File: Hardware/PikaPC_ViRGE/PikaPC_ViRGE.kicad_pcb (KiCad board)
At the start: 4 copper layers, 101.6 x 101.6 mm, 136 parts, among them J1 Conn_02x07_Odd_Even, J2 DIN41612_03x32_C_Split, J3 Conn_02x08_Odd_Even, J4 DE15_Socket_HighDensity_Mount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, U1 ATF1504, U10 74LS573, U12 74FCT2245, U13 74FCT2245, U14 74FCT2245, U15 74FCT2245, U2 86C325, U3 74F521, U4 T224162B, U5 T224162B, U6 T224162B, U7 T224162B, U8 74LS573, U9 74LS573, Y1 14M31818

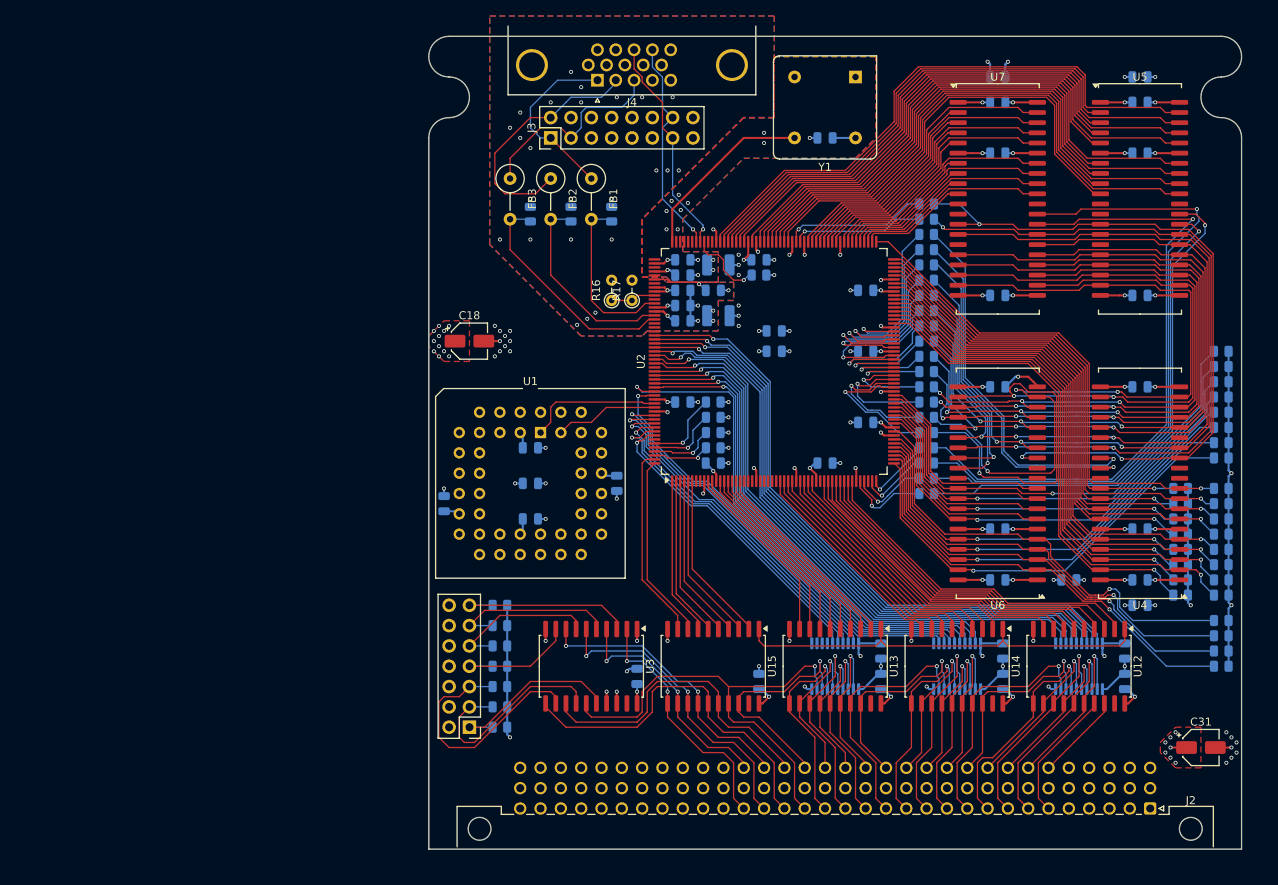
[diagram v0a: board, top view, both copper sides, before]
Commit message: ViRGE card PCB layout
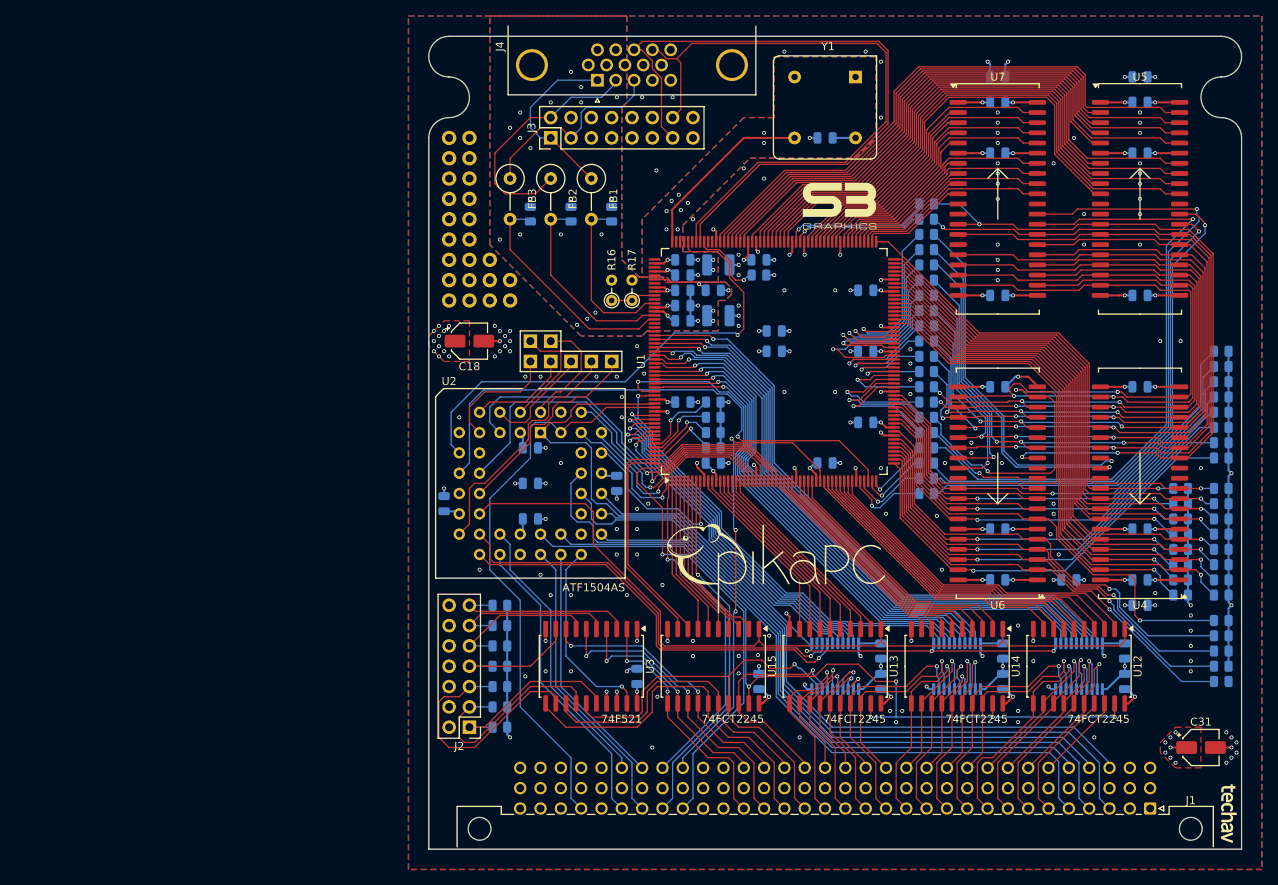
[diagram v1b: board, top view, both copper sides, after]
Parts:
- added IO11: TestPoint, Connector_PinHeader_2.54mm:PinHeader_1x01_P2.54mm_Vertical, B.Cu at (91.4, 66.0)
- added IO16: TestPoint, Connector_PinHeader_2.54mm:PinHeader_1x01_P2.54mm_Vertical, B.Cu at (94.0, 66.0)
- added IO2: TestPoint, Connector_PinHeader_2.54mm:PinHeader_1x01_P2.54mm_Vertical, B.Cu at (88.9, 63.5)
- added IO24: TestPoint, Connector_PinHeader_2.54mm:PinHeader_1x01_P2.54mm_Vertical, B.Cu at (96.5, 66.0)
- added IO30: TestPoint, Connector_PinHeader_2.54mm:PinHeader_1x01_P2.54mm_Vertical, B.Cu at (99.1, 66.0)
- added IO44: TestPoint, Connector_PinHeader_2.54mm:PinHeader_1x01_P2.54mm_Vertical, B.Cu at (91.4, 63.5)
- added IO5: TestPoint, Connector_PinHeader_2.54mm:PinHeader_1x01_P2.54mm_Vertical, B.Cu at (88.9, 66.0)
- added REF**: PinHeader_1x01_P2.54mm_Vertical, Connector_PinHeader_2.54mm:PinHeader_1x01_P2.54mm_Vertical, F.Cu at (78.7, 43.2)
- added REF**: PinHeader_1x01_P2.54mm_Vertical, Connector_PinHeader_2.54mm:PinHeader_1x01_P2.54mm_Vertical, F.Cu at (81.3, 45.7)
- added REF**: PinHeader_1x01_P2.54mm_Vertical, Connector_PinHeader_2.54mm:PinHeader_1x01_P2.54mm_Vertical, F.Cu at (78.7, 38.1)
- added REF**: PinHeader_1x01_P2.54mm_Vertical, Connector_PinHeader_2.54mm:PinHeader_1x01_P2.54mm_Vertical, F.Cu at (78.7, 48.3)
- added REF**: PinHeader_1x01_P2.54mm_Vertical, Connector_PinHeader_2.54mm:PinHeader_1x01_P2.54mm_Vertical, F.Cu at (78.7, 50.8)
- added REF**: PinHeader_1x01_P2.54mm_Vertical, Connector_PinHeader_2.54mm:PinHeader_1x01_P2.54mm_Vertical, F.Cu at (86.4, 58.4)
- added REF**: PinHeader_1x01_P2.54mm_Vertical, Connector_PinHeader_2.54mm:PinHeader_1x01_P2.54mm_Vertical, F.Cu at (81.3, 48.3)
- added REF**: PinHeader_1x01_P2.54mm_Vertical, Connector_PinHeader_2.54mm:PinHeader_1x01_P2.54mm_Vertical, F.Cu at (81.3, 43.2)
- added REF**: PinHeader_1x01_P2.54mm_Vertical, Connector_PinHeader_2.54mm:PinHeader_1x01_P2.54mm_Vertical, F.Cu at (81.3, 55.9)
- added REF**: PinHeader_1x01_P2.54mm_Vertical, Connector_PinHeader_2.54mm:PinHeader_1x01_P2.54mm_Vertical, F.Cu at (78.7, 55.9)
- added REF**: PinHeader_1x01_P2.54mm_Vertical, Connector_PinHeader_2.54mm:PinHeader_1x01_P2.54mm_Vertical, F.Cu at (81.3, 50.8)
- added REF**: PinHeader_1x01_P2.54mm_Vertical, Connector_PinHeader_2.54mm:PinHeader_1x01_P2.54mm_Vertical, F.Cu at (78.7, 58.4)
- added REF**: PinHeader_1x01_P2.54mm_Vertical, Connector_PinHeader_2.54mm:PinHeader_1x01_P2.54mm_Vertical, F.Cu at (83.8, 53.3)
- added REF**: PinHeader_1x01_P2.54mm_Vertical, Connector_PinHeader_2.54mm:PinHeader_1x01_P2.54mm_Vertical, F.Cu at (81.3, 53.3)
- added REF**: PinHeader_1x01_P2.54mm_Vertical, Connector_PinHeader_2.54mm:PinHeader_1x01_P2.54mm_Vertical, F.Cu at (78.7, 45.7)
- added REF**: PinHeader_1x01_P2.54mm_Vertical, Connector_PinHeader_2.54mm:PinHeader_1x01_P2.54mm_Vertical, F.Cu at (78.7, 40.6)
- added REF**: PinHeader_1x01_P2.54mm_Vertical, Connector_PinHeader_2.54mm:PinHeader_1x01_P2.54mm_Vertical, F.Cu at (83.8, 55.9)
- added REF**: PinHeader_1x01_P2.54mm_Vertical, Connector_PinHeader_2.54mm:PinHeader_1x01_P2.54mm_Vertical, F.Cu at (81.3, 38.1)
- added REF**: PinHeader_1x01_P2.54mm_Vertical, Connector_PinHeader_2.54mm:PinHeader_1x01_P2.54mm_Vertical, F.Cu at (78.7, 53.3)
- added REF**: PinHeader_1x01_P2.54mm_Vertical, Connector_PinHeader_2.54mm:PinHeader_1x01_P2.54mm_Vertical, F.Cu at (81.3, 40.6)
- added REF**: PinHeader_1x01_P2.54mm_Vertical, Connector_PinHeader_2.54mm:PinHeader_1x01_P2.54mm_Vertical, F.Cu at (81.3, 58.4)
- added REF**: PinHeader_1x01_P2.54mm_Vertical, Connector_PinHeader_2.54mm:PinHeader_1x01_P2.54mm_Vertical, F.Cu at (83.8, 58.4)
- added REF**: PinHeader_1x01_P2.54mm_Vertical, Connector_PinHeader_2.54mm:PinHeader_1x01_P2.54mm_Vertical, F.Cu at (86.4, 55.9)
- added SR28: 10K, Resistor_SMD:R_0805_2012Metric, B.Cu at (175.3, 98.4)
- U10, U8, U9: value 74LS573 -> 74AHCT573
- U2: renamed from U1; value ATF1504 -> ATF1504AS
- moved SR24 1.91 mm to (175.3, 106.0)
- moved SR25 1.91 mm to (175.3, 104.1)
- moved SR26 1.91 mm to (175.3, 102.2)
- moved SR27 1.91 mm to (175.3, 100.3)
- renumbered J2 to J1, J1 to J2, R38 to SR00, R39 to SR01, R40 to SR02, R41 to SR03, R42 to SR04, R43 to SR05, R44 to SR06, R45 to SR07, R46 to SR08, R47 to SR09, R48 to SR10, R49 to SR11, R50 to SR12, R51 to SR13, R52 to SR14, R53 to SR15, R54 to SR16, R55 to SR17, R56 to SR18, R57 to SR19, R58 to SR20, R59 to SR21, R60 to SR22, R61 to SR23, R62 to SR24, R63 to SR25, R64 to SR26, R65 to SR27, U2 to U1
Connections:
- U2 pad 11: /Main Bus/~{Bus-IRQ1} -> /Main Bus/VID-SAUP2
- U2 pad 12: /Main Bus/~{Bus-IRQ0} -> /Main Bus/~{OE}
- U2 pad 14: /Main Bus/~{AEN} -> Net-(U2A-IO30)
- U2 pad 17: /Main Bus/~{BEN} -> Net-(U2A-IO24)
- U2 pad 18: /Main Bus/~{Bus-Start} -> /Main Bus/A23
- U2 pad 19: /Main Bus/~{Bus-ACK} -> /Main Bus/A24
- U2 pad 2: unconnected-(U1A-OE2/GCLK2-Pad2) -> Net-(U2A-OE2/GCLK2)
- U2 pad 20: /Main Bus/Bus-R/~{W} -> /Main Bus/~{Bus-ACK}
- U2 pad 21: unconnected-(U1A-IO17-Pad21) -> /Main Bus/~{Bus-Start}
- U2 pad 24: /Main Bus/VID-SAUP1 -> /Main Bus/~{Bus-BURST}
- U2 pad 25: /Main Bus/VID-SAUP2 -> /Main Bus/~{BEN}
- U2 pad 26: /Main Bus/A23 -> /Main Bus/~{Bus-BRACK}
- U2 pad 27: /Main Bus/A24 -> /Main Bus/~{Bus-IRQ2}
- U2 pad 29: /Main Bus/VID-M/~{IO} -> /Main Bus/~{Bus-IRQ1}
- U2 pad 31: /Main Bus/~{OE} -> /Main Bus/~{Bus-IRQ0}
- U2 pad 33: /Main Bus/~{VID-ADS} -> /Main Bus/~{AEN}
- U2 pad 34: /Main Bus/~{VID-RDYIN} -> /Main Bus/~{Bus-IACK}
- U2 pad 36: /Main Bus/~{VID-SRDY} -> /Main Bus/Bus-R/~{W}
- U2 pad 37: /Main Bus/INT0 -> /Main Bus/VID-M/~{IO}
- U2 pad 39: unconnected-(U1A-IO57-Pad39) -> /Main Bus/~{VID-RDYIN}
- U2 pad 4: unconnected-(U1A-IO16-Pad4) -> Net-(U2A-IO16)
- U2 pad 40: unconnected-(U1A-IO62-Pad40) -> /Main Bus/~{VID-SRDY}
- U2 pad 41: unconnected-(U1A-IO64-Pad41) -> /Main Bus/~{VID-ADS}
- U2 pad 44: unconnected-(U1A-OE1-Pad44) -> Net-(U2A-OE1)
- U2 pad 5: /Main Bus/~{Bus-BRACK} -> /Main Bus/VID-SAUP1
- U2 pad 6: /Main Bus/~{Bus-BURST} -> Net-(U2A-IO11)
- U2 pad 8: /Main Bus/~{Bus-IACK} -> Net-(U2A-IO5)
- U2 pad 9: /Main Bus/~{Bus-IRQ2} -> /Main Bus/INT0
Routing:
- net /Main Bus/~{BEN}: track 0.00 -> 102.0 mm, vias 0 -> 5
- net /Main Bus/~{Bus-Reset}: track 17.0 -> 112.9 mm
- net /Main Bus/Bus-R/~{W}: track 0.00 -> 86.8 mm
- net /Main Bus/~{Bus-IRQ0}: track 0.00 -> 85.5 mm
- net /Main Bus/~{Bus-IRQ2}: track 0.00 -> 84.8 mm
- net /Main Bus/~{Bus-IACK}: track 0.00 -> 83.8 mm
- net /Main Bus/~{Bus-IRQ1}: track 0.00 -> 82.1 mm
- net /Main Bus/~{Bus-BE1}: track 0.00 -> 73.9 mm, vias 0 -> 1
- net /Main Bus/~{AEN}: track 0.00 -> 68.9 mm, vias 0 -> 3
- net /Main Bus/VID-SAUP2: track 0.00 -> 68.1 mm, vias 0 -> 1
- net /Main Bus/INT0: track 0.00 -> 62.3 mm, vias 0 -> 1
- net /Main Bus/Bus-Clk: track 13.0 -> 72.1 mm
- net /Video/Vid-H: track 27.7 -> 86.2 mm, vias 1 -> 0
- net /Main Bus/~{Bus-BE0}: track 0.00 -> 58.2 mm, vias 0 -> 3
- net /Main Bus/~{Bus-BE2}: track 0.00 -> 55.7 mm, vias 0 -> 1
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- added copper zone on B.Cu, net GND
- added copper zone on F.Cu, net GND
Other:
- board text added: "33Ω"
- board text added: "75Ω"
- board text added: "SR[01:00] Bus Select SR[03:02] Page Mode SR[04] Enable VBIOS SR[07:05] VRAM Size SR[08] VGA Enable SR[09] Reserved SR[10] VBIOS Size SR[11] DCLK/MCLK Src SR[12] RAMDAC ~{LOCA}"
- board text added: "SR[15:15] Reserved SR[17:16] ~{CAS}/~{OE} Adjust SR[18] ~{RAS} Timing SR[19] ~{RAS} Pre-charge SR[23:20] Reserved SR[24] Trio LPB Mode SR[25] Serial Address SR[26] MMIO Serial SR[28:27] ~{WE} Delay"
- board text added: "Strapping Options (10kΩ)"

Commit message: Un-assign main bus pins 22 & 23
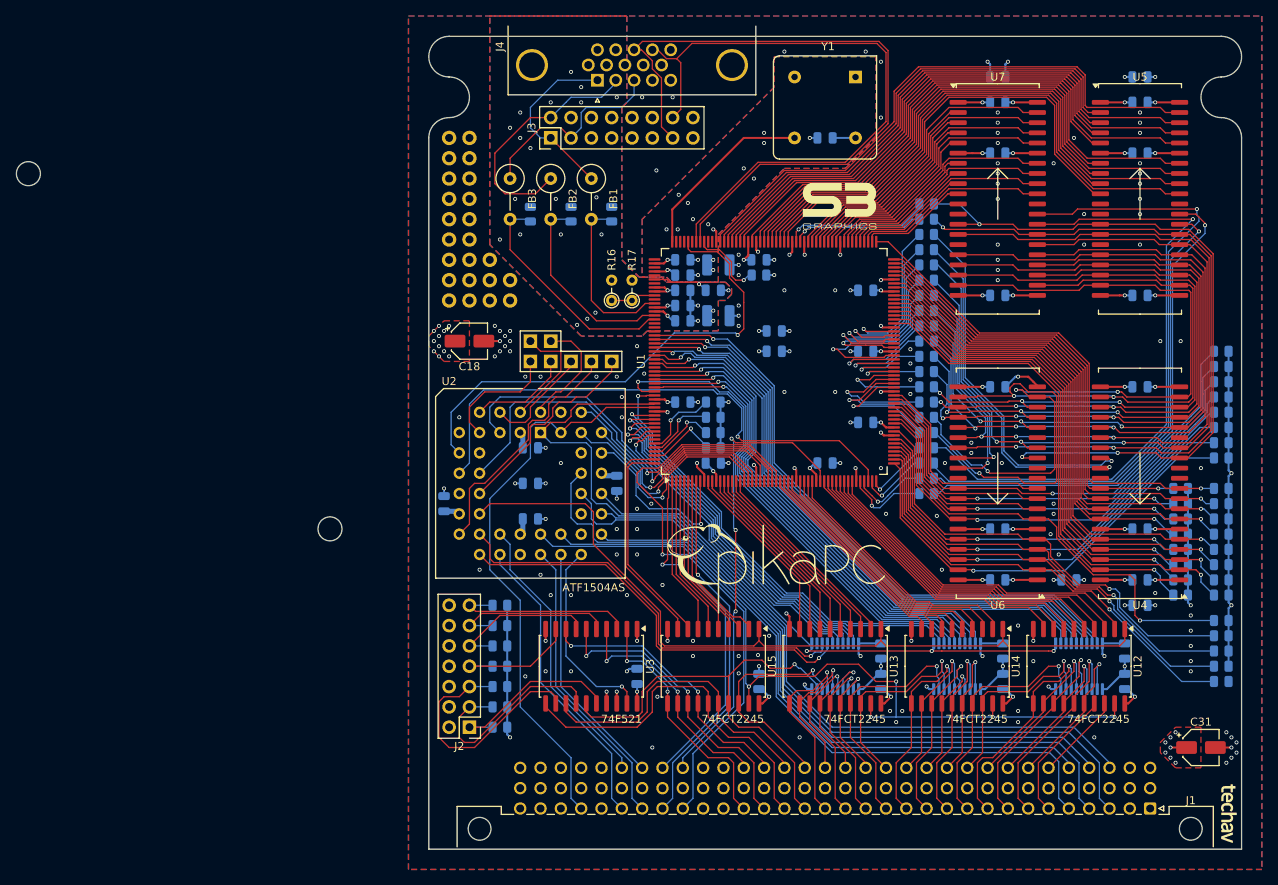
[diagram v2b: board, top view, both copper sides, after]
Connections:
- J1 pad b22: GND -> unconnected-(J1B-Pin_b22-Padb22)
- J1 pad b23: GND -> unconnected-(J1B-Pin_b23-Padb23)
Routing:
- net /Main Bus/~{Bus-BE2}: track 55.7 -> 57.0 mm
- net GND1: vias 14 -> 15
- net GND: vias 193 -> 190
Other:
- board size 101.6 x 101.6 mm -> 153.2 x 101.6 mm

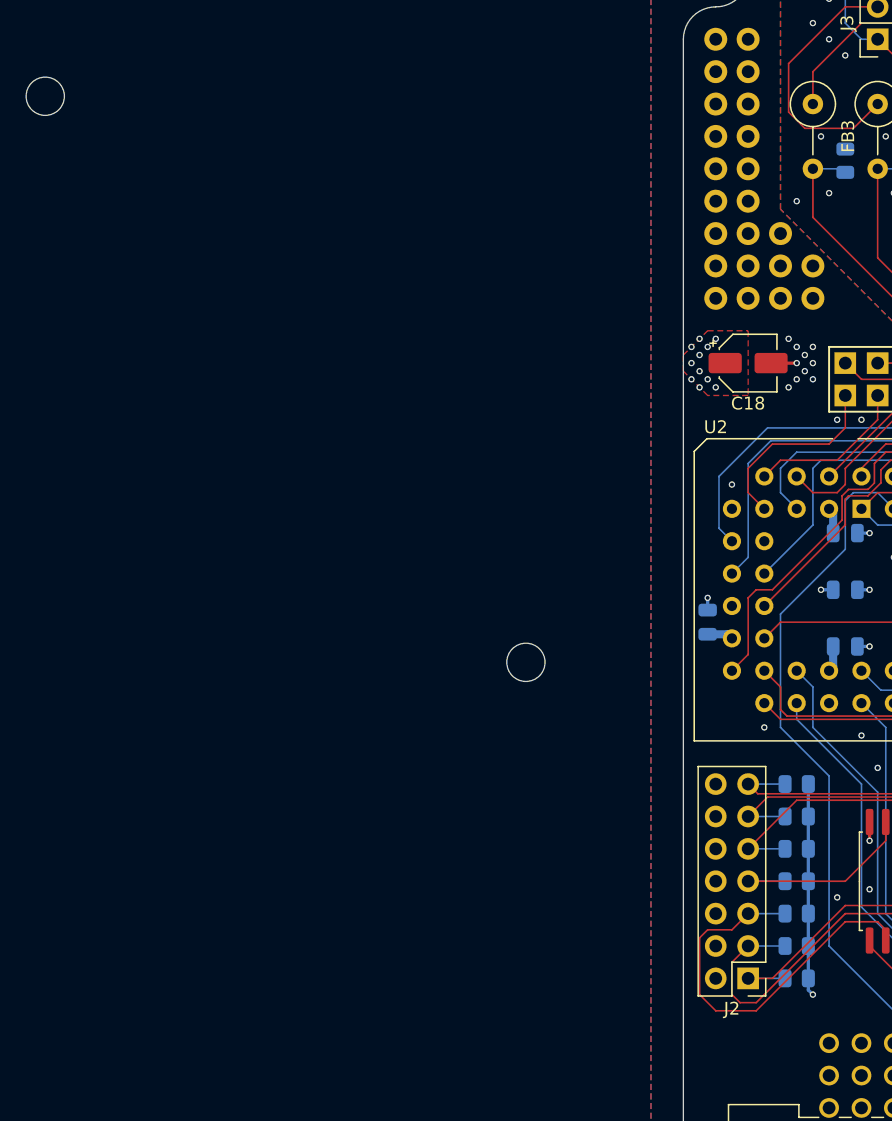
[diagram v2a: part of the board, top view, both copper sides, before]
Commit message: Silkscreen cleanup
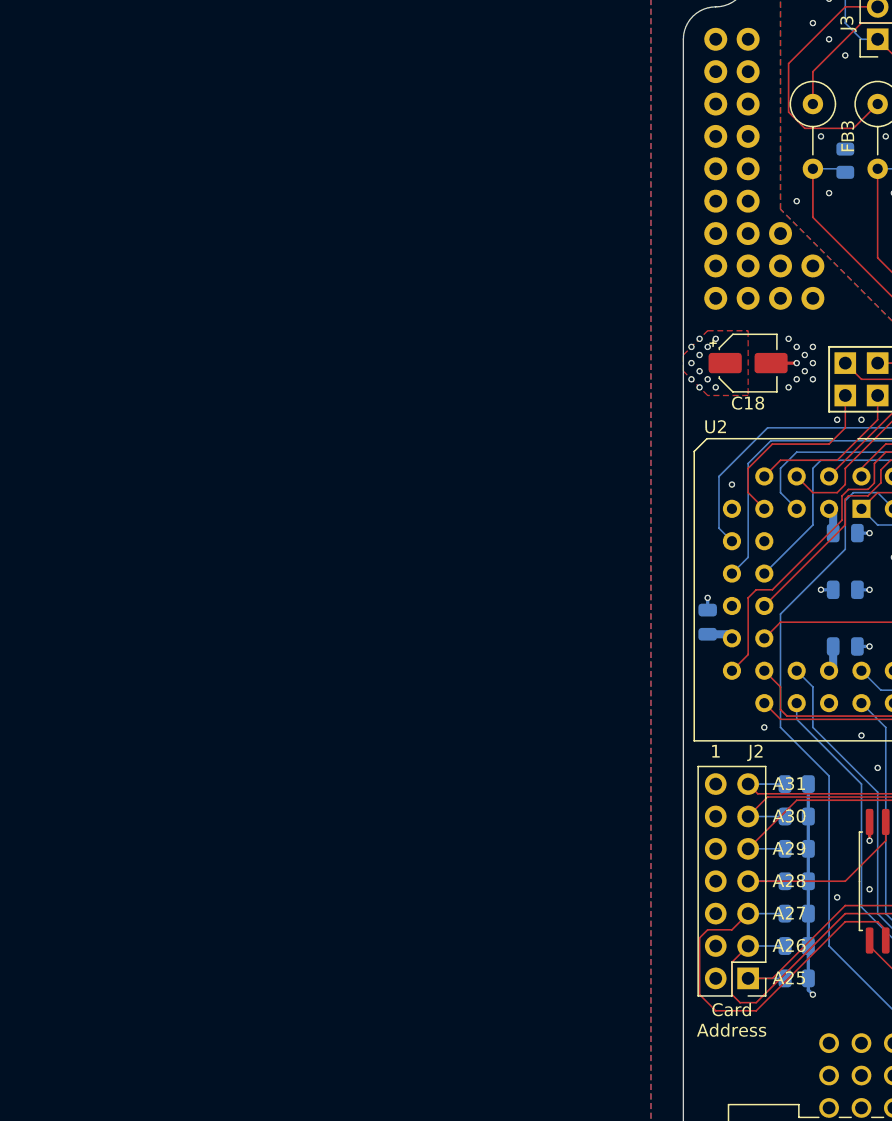
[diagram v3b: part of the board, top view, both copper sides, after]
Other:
- board size 153.2 x 101.6 mm -> 101.6 x 101.6 mm
- board text added: "1"
- board text added: "A25"
- board text added: "A26"
- board text added: "A27"
- board text added: "A28"
- board text added: "A29"
- board text added: "A30"
- board text added: "A31"
- board text added: "Card Address"
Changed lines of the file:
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@@
 		(tags "Through hole pin header THT 2x07 2.54mm double row")
 		(property "Reference" "J2"
-			(at 1.27 -2.380001 0)
+			(at -0.635 17.78 0)
 			(layer "F.SilkS")
 			(effects
@@
 		(layer "Edge.Cuts")
 	)
-	(gr_circle
-		(center 63.85 86.97)
-		(end 63.85 85.47)
-		(stroke
-			(width 0.1)
-			(type default)
-		)
-		(fill no)
-		(layer "Edge.Cuts")
-	)
 	(gr_line
 		(start 76.2 127.000001)
@@
 		(layer "Edge.Cuts")
 	)
-	(gr_circle
-		(center 26.15 42.57)
-		(end 26.15 41.07)
-		(stroke
-			(width 0.1)
-			(type default)
-		)
-		(fill no)
-		(layer "Edge.Cuts")
-	)
 	(gr_line
 		(start 177.8 127.000001)
@@
 		(layer "Edge.Cuts")
 	)
-	(gr_line
-		(start 23.15 89.97)
-		(end 23.15 39.57)
-		(stroke
-			(width 0.15)
-			(type default)
-		)
-		(layer "User.2")
-	)
-	(gr_line
-		(start 66.85 39.57)
-		(end 66.85 89.97)
-		(stroke
-			(width 0.15)
-			(type default)
+	(gr_text "A26"
+		(at 83.185 109.22 0)
+		(layer "F.SilkS")
+		(effects
+			(font
+				(size 1 1)
+				(thickness 0.15)
+			)
+			(justify left)
 		)
-		(layer "User.2")
 	)
-	(gr_line
-		(start 23.15 89.97)
-		(end 66.85 89.97)
-		(stroke
-			(width 0.15)
-			(type default)
+	(gr_text "A25"
+		(at 83.185 111.76 0)
+		(layer "F.SilkS")
+		(effects
+			(font
+				(size 1 1)
+				(thickness 0.15)
+			)
+			(justify left)
 		)
-		(layer "User.2")
 	)
-	(gr_line
-		(start 66.85 39.57)
-		(end 23.15 39.57)
-		(stroke
-			(width 0.15)
-			(type default)
+	(gr_text "A29"
+		(at 83.185 101.6 0)
+		(layer "F.SilkS")
+		(effects
+			(font
+				(size 1 1)
+				(thickness 0.15)
+			)
+			(justify left)
 		)
-		(layer "User.2")
 	)
-	(gr_line
-		(start 23.15 86.97)
-		(end 66.85 86.97)
-		(stroke
-			(width 0.15)
-			(type default)
+	(gr_text "A27"
+		(at 83.185 106.68 0)
+		(layer "F.SilkS")
+		(effects
+			(font
+				(size 1 1)
+				(thickness 0.15)
+			)
+			(justify left)
 		)
-		(layer "User.3")
 	)
-	(gr_line
-		(start 23.15 42.57)
-		(end 66.85 42.57)
-		(stroke
-			(width 0.15)
-			(type default)
+	(gr_text "Card\nAddress"
+		(at 80.01 113.665 0)
+		(layer "F.SilkS")
+		(effects
+			(font
+				(size 1 1)
+				(thickness 0.15)
+			)
+			(justify top)
 		)
-		(layer "User.3")
 	)
-	(gr_line
-		(start 63.85 39.57)
-		(end 63.85 89.97)
-		(stroke
-			(width 0.15)
-			(type default)
+	(gr_text "A30"
+		(at 83.185 99.06 0)
+		(layer "F.SilkS")
+		(effects
+			(font
+				(size 1 1)
+				(thickness 0.15)
+			)
+			(justify left)
 		)
-		(layer "User.3")
 	)
-	(gr_line
-		(start 66.85 89.97)
-		(end 23.15 39.57)
-		(stroke
-			(width 0.15)
-			(type default)
+	(gr_text "A31"
+		(at 83.185 96.52 0)
+		(layer "F.SilkS")
+		(effects
+			(font
+				(size 1 1)
+				(thickness 0.15)
+			)
+			(justify left)
 		)
-		(layer "User.3")
 	)
-	(gr_line
-		(start 23.15 89.97)
-		(end 66.85 39.57)
-		(stroke
-			(width 0.15)
-			(type default)
+	(gr_text "1"
+		(at 78.74 93.98 0)
+		(layer "F.SilkS")
+		(effects
+			(font
+				(size 1 1)
+				(thickness 0.15)
+			)
 		)
-		(layer "User.3")
 	)
-	(gr_line
-		(start 26.15 39.57)
-		(end 26.15 89.97)
-		(stroke
-			(width 0.15)
-			(type default)
+	(gr_text "A28"
+		(at 83.185 104.14 0)
+		(layer "F.SilkS")
+		(effects
+			(font
+				(size 1 1)
+				(thickness 0.15)
+			)
+			(justify left)
 		)
-		(layer "User.3")
 	)
 	(gr_text "SR[15:15] Reserved\nSR[17:16] ~{CAS}/~{OE} Adjust\nSR[18]    ~{RAS} Timing\nSR[19]    ~{RAS} Pre-charge\nSR[23:20] Reserved\nSR[24]    Trio LPB Mode\nSR[25]    Serial Address\nSR[26]    MMIO Serial\nSR[28:27] ~{WE} Delay"
@@
 		)
 	)
-	(group ""
-		(members "1f4588c8-13db-436d-9268-01f02a069088" "3f969e69-6c27-447f-bb0f-0ecb9cc801a8"
-			"4199aa02-bd0a-4f9d-9ee8-4bd1605c11e3" "44c5f483-8cdb-4863-9151-b4f97b87447d"
-			"5d5e2638-9819-4c1e-8c54-5f082c90af25" "708932de-779c-4a88-a98f-0296514352e0"
-			"74ca7d4d-9157-4ece-98d2-67ccadffb7c4" "7501eb56-1376-4929-a8f8-fa415166ef4e"
-			"a56dcdf0-7b99-4cf2-814f-352ae971e921" "d590a308-9a78-4108-9b2f-e51c4c010284"
-			"d751e56a-613e-43d4-8886-a5e6f029482e" "f386f4af-4028-4b77-8a44-1f5f43a01333"
-		)
-	)
